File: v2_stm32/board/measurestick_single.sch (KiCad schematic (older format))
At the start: 5 parts, among them IC1 LM393, J1 USB_A

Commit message: STM32 board: Power supply
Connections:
- wire segments 24 -> 19
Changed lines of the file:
@@
 $Descr A4 11693 8268
 encoding utf-8
-Sheet 4 5
+Sheet 3 6
 Title ""
 Date ""
@@
 	1    0    0    -1
 $EndComp
-Wire Wire Line
-	4850 2700 4850 2750
-Wire Wire Line
-	4850 3350 4850 3400
 $Comp
 L power:GND #PWR?
 U 1 1 60261649
-P 4850 3400
+P 4850 3350
 AR Path="/60261649" Ref="#PWR?"  Part="1"
 AR Path="/6025D9E2/60261649" Ref="#PWR?"  Part="1"
@@
 AR Path="/60265FC9/60261649" Ref="#PWR?"  Part="1"
 AR Path="/6026601C/60261649" Ref="#PWR?"  Part="1"
-F 0 "#PWR?" H 4850 3150 50  0001 C CNN
-F 1 "GND" H 4855 3227 50  0000 C CNN
-F 2 "" H 4850 3400 50  0001 C CNN
-F 3 "" H 4850 3400 50  0001 C CNN
-	1    4850 3400
+F 0 "#PWR?" H 4850 3100 50  0001 C CNN
+F 1 "GND" H 4855 3177 50  0000 C CNN
+F 2 "" H 4850 3350 50  0001 C CNN
+F 3 "" H 4850 3350 50  0001 C CNN
+	1    4850 3350
 	1    0    0    -1
 $EndComp
@@
 L power:GND #PWR?
 U 1 1 60261663
-P 2300 3450
+P 2300 3400
 AR Path="/6025D9E2/60261663" Ref="#PWR?"  Part="1"
 AR Path="/6025D9E2/6025E7C0/60261663" Ref="#PWR01"  Part="1"
@@
 AR Path="/60265FC9/60261663" Ref="#PWR?"  Part="1"
 AR Path="/6026601C/60261663" Ref="#PWR?"  Part="1"
-F 0 "#PWR?" H 2300 3200 50  0001 C CNN
-F 1 "GND" H 2305 3277 50  0000 C CNN
-F 2 "" H 2300 3450 50  0001 C CNN
-F 3 "" H 2300 3450 50  0001 C CNN
-	1    2300 3450
-	1    0    0    -1
-$EndComp
-Wire Wire Line
-	2300 3400 2300 3450
+F 0 "#PWR?" H 2300 3150 50  0001 C CNN
+F 1 "GND" H 2305 3227 50  0000 C CNN
+F 2 "" H 2300 3400 50  0001 C CNN
+F 3 "" H 2300 3400 50  0001 C CNN
+	1    2300 3400
+	1    0    0    -1
+$EndComp
 Connection ~ 2300 3400
 Wire Wire Line
@@
 Text HLabel 4250 3450 2    50   Input ~ 0
 CLK
-$Comp
-L power:+3.3V #PWR?
-U 1 1 60261675
-P 4850 2700
-AR Path="/6025D9E2/60261675" Ref="#PWR?"  Part="1"
-AR Path="/6025D9E2/6025E7C0/60261675" Ref="#PWR05"  Part="1"
-AR Path="/6025D9E2/60265A76/60261675" Ref="#PWR?"  Part="1"
-AR Path="/6025D9E2/60265B58/60261675" Ref="#PWR?"  Part="1"
-AR Path="/6025D9E2/60265BB4/60261675" Ref="#PWR?"  Part="1"
-AR Path="/6025D9E2/60265C25/60261675" Ref="#PWR?"  Part="1"
-AR Path="/60265C89/60261675" Ref="#PWR?"  Part="1"
-AR Path="/60265F6D/60261675" Ref="#PWR?"  Part="1"
-AR Path="/60265FC9/60261675" Ref="#PWR?"  Part="1"
-AR Path="/6026601C/60261675" Ref="#PWR?"  Part="1"
-F 0 "#PWR?" H 4850 2550 50  0001 C CNN
-F 1 "+3.3V" H 4865 2873 50  0000 C CNN
-F 2 "" H 4850 2700 50  0001 C CNN
-F 3 "" H 4850 2700 50  0001 C CNN
-	1    4850 2700
-	1    0    0    -1
-$EndComp
 $Comp
 L Device:R R?
@@
 L power:+3.3V #PWR?
 U 1 1 60261690
-P 3400 2100
+P 3400 2150
 AR Path="/6025D9E2/60261690" Ref="#PWR?"  Part="1"
 AR Path="/6025D9E2/6025E7C0/60261690" Ref="#PWR03"  Part="1"
@@
 AR Path="/60265FC9/60261690" Ref="#PWR?"  Part="1"
 AR Path="/6026601C/60261690" Ref="#PWR?"  Part="1"
-F 0 "#PWR?" H 3400 1950 50  0001 C CNN
-F 1 "+3.3V" H 3415 2273 50  0000 C CNN
-F 2 "" H 3400 2100 50  0001 C CNN
-F 3 "" H 3400 2100 50  0001 C CNN
-	1    3400 2100
+F 0 "#PWR?" H 3400 2000 50  0001 C CNN
+F 1 "+3.3V" H 3415 2323 50  0000 C CNN
+F 2 "" H 3400 2150 50  0001 C CNN
+F 3 "" H 3400 2150 50  0001 C CNN
+	1    3400 2150
 	1    0    0    -1
 $EndComp
@@
 L power:GND #PWR?
 U 1 1 60261696
-P 3400 3950
+P 3400 3900
 AR Path="/60261696" Ref="#PWR?"  Part="1"
 AR Path="/6025D9E2/60261696" Ref="#PWR?"  Part="1"
@@
 AR Path="/60265FC9/60261696" Ref="#PWR?"  Part="1"
 AR Path="/6026601C/60261696" Ref="#PWR?"  Part="1"
-F 0 "#PWR?" H 3400 3700 50  0001 C CNN
-F 1 "GND" H 3405 3777 50  0000 C CNN
-F 2 "" H 3400 3950 50  0001 C CNN
-F 3 "" H 3400 3950 50  0001 C CNN
-	1    3400 3950
-	1    0    0    -1
-$EndComp
-Wire Wire Line
-	3400 3900 3400 3950
-Wire Wire Line
-	3400 2150 3400 2100
+F 0 "#PWR?" H 3400 3650 50  0001 C CNN
+F 1 "GND" H 3405 3727 50  0000 C CNN
+F 2 "" H 3400 3900 50  0001 C CNN
+F 3 "" H 3400 3900 50  0001 C CNN
+	1    3400 3900
+	1    0    0    -1
+$EndComp
 $Comp
 L Device:C C?
@@
 L power:+3.3V #PWR?
 U 1 1 602616A5
-P 5400 2700
+P 5400 2750
 AR Path="/6025D9E2/602616A5" Ref="#PWR?"  Part="1"
 AR Path="/6025D9E2/6025E7C0/602616A5" Ref="#PWR07"  Part="1"
@@
 AR Path="/60265FC9/602616A5" Ref="#PWR?"  Part="1"
 AR Path="/6026601C/602616A5" Ref="#PWR?"  Part="1"
-F 0 "#PWR?" H 5400 2550 50  0001 C CNN
-F 1 "+3.3V" H 5415 2873 50  0000 C CNN
-F 2 "" H 5400 2700 50  0001 C CNN
-F 3 "" H 5400 2700 50  0001 C CNN
-	1    5400 2700
+F 0 "#PWR?" H 5400 2600 50  0001 C CNN
+F 1 "+3.3V" H 5415 2923 50  0000 C CNN
+F 2 "" H 5400 2750 50  0001 C CNN
+F 3 "" H 5400 2750 50  0001 C CNN
+	1    5400 2750
 	1    0    0    -1
 $EndComp
@@
 L power:GND #PWR?
 U 1 1 602616AB
-P 5400 3400
+P 5400 3350
 AR Path="/602616AB" Ref="#PWR?"  Part="1"
 AR Path="/6025D9E2/602616AB" Ref="#PWR?"  Part="1"
@@
 AR Path="/60265FC9/602616AB" Ref="#PWR?"  Part="1"
 AR Path="/6026601C/602616AB" Ref="#PWR?"  Part="1"
-F 0 "#PWR?" H 5400 3150 50  0001 C CNN
-F 1 "GND" H 5405 3227 50  0000 C CNN
-F 2 "" H 5400 3400 50  0001 C CNN
-F 3 "" H 5400 3400 50  0001 C CNN
-	1    5400 3400
-	1    0    0    -1
-$EndComp
-Wire Wire Line
-	5400 3200 5400 3400
-Wire Wire Line
-	5400 2700 5400 2900
+F 0 "#PWR?" H 5400 3100 50  0001 C CNN
+F 1 "GND" H 5405 3177 50  0000 C CNN
+F 2 "" H 5400 3350 50  0001 C CNN
+F 3 "" H 5400 3350 50  0001 C CNN
+	1    5400 3350
+	1    0    0    -1
+$EndComp
+Wire Wire Line
+	5400 3200 5400 3350
+Wire Wire Line
+	5400 2750 5400 2900
+$Comp
+L power:+3.3V #PWR?
+U 1 1 60261675
+P 4850 2750
+AR Path="/6025D9E2/60261675" Ref="#PWR?"  Part="1"
+AR Path="/6025D9E2/6025E7C0/60261675" Ref="#PWR05"  Part="1"
+AR Path="/6025D9E2/60265A76/60261675" Ref="#PWR?"  Part="1"
+AR Path="/6025D9E2/60265B58/60261675" Ref="#PWR?"  Part="1"
+AR Path="/6025D9E2/60265BB4/60261675" Ref="#PWR?"  Part="1"
+AR Path="/6025D9E2/60265C25/60261675" Ref="#PWR?"  Part="1"
+AR Path="/60265C89/60261675" Ref="#PWR?"  Part="1"
+AR Path="/60265F6D/60261675" Ref="#PWR?"  Part="1"
+AR Path="/60265FC9/60261675" Ref="#PWR?"  Part="1"
+AR Path="/6026601C/60261675" Ref="#PWR?"  Part="1"
+F 0 "#PWR?" H 4850 2600 50  0001 C CNN
+F 1 "+3.3V" H 4865 2923 50  0000 C CNN
+F 2 "" H 4850 2750 50  0001 C CNN
+F 3 "" H 4850 2750 50  0001 C CNN
+	1    4850 2750
+	1    0    0    -1
+$EndComp
 $EndSCHEMATC

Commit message: Switched to 64 pin STM32F103. Assigned pins
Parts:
- J1: symbol Connector:USB_A -> lathecontrol_stm32-rescue:USB_A-Connector
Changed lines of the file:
@@
 IN_Clk
 $Comp
-L Connector:USB_A J?
+L lathecontrol_stm32-rescue:USB_A-Connector J?
 U 1 1 60261659
 P 2350 3000
@@
 AR Path="/60265FC9/60261659" Ref="J?"  Part="1"
 AR Path="/6026601C/60261659" Ref="J?"  Part="1"
+AR Path="/60261659" Ref="J?"  Part="1"
 F 0 "J?" H 2407 3467 50  0000 C CNN
 F 1 "USB_A" H 2407 3376 50  0000 C CNN

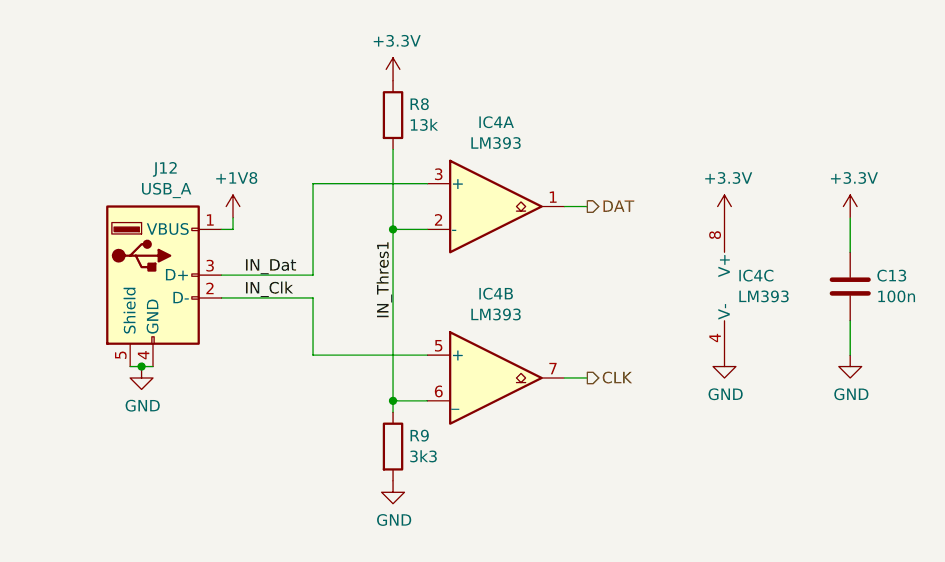
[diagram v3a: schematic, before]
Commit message: Added connectors
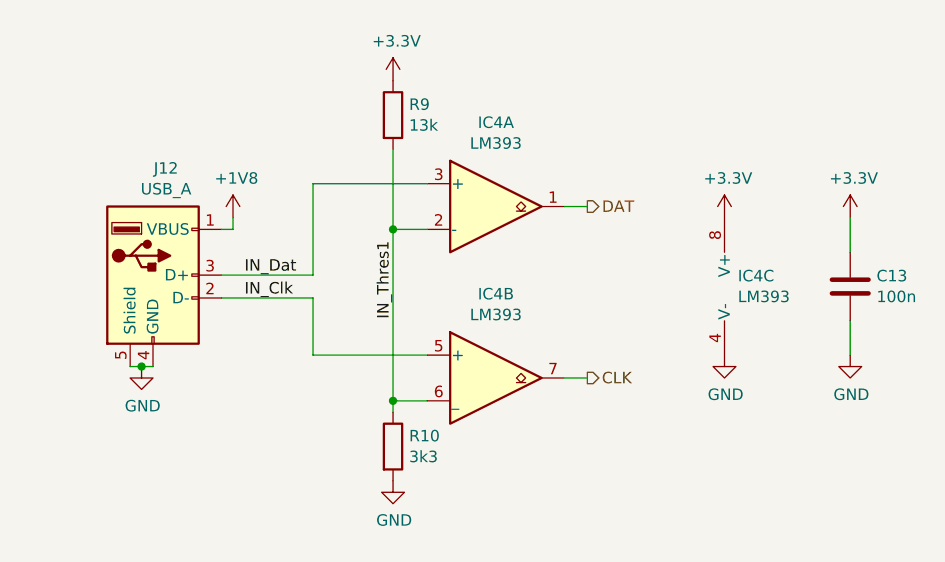
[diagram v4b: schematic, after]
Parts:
- renumbered C1 to C10, J1 to J9, R1 to R3, R2 to R4

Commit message: Added LEDs
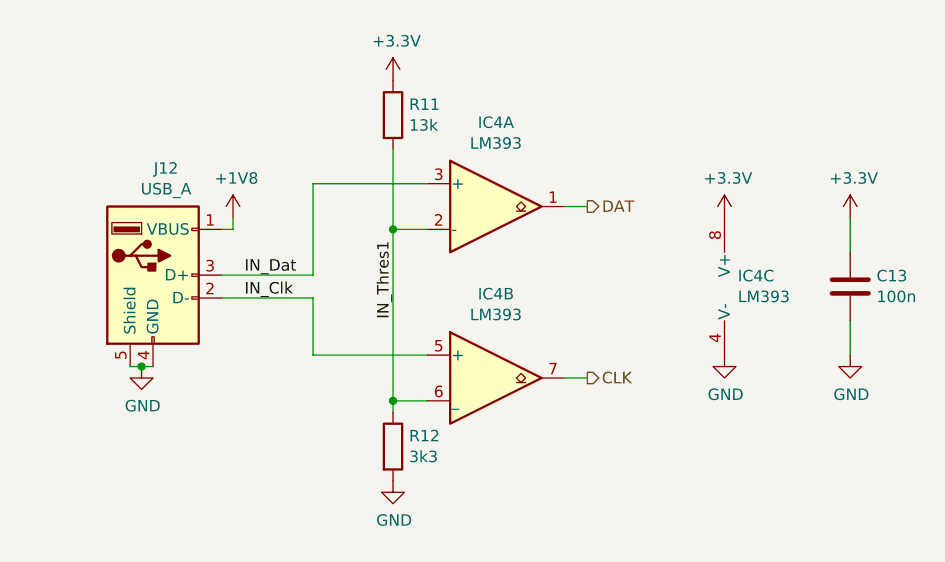
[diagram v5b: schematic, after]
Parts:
- renumbered R3 to R5, R4 to R6
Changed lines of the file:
@@
 AR Path="/6025D9E2/60265BB4/60261649" Ref="#PWR?"  Part="1"
 AR Path="/6025D9E2/60265C25/60261649" Ref="#PWR?"  Part="1"
-AR Path="/60265C89/60261649" Ref="#PWR040"  Part="1"
-AR Path="/60265F6D/60261649" Ref="#PWR048"  Part="1"
-AR Path="/60265FC9/60261649" Ref="#PWR056"  Part="1"
-AR Path="/6026601C/60261649" Ref="#PWR064"  Part="1"
-F 0 "#PWR064" H 4850 3100 50  0001 C CNN
+AR Path="/60265C89/60261649" Ref="#PWR042"  Part="1"
+AR Path="/60265F6D/60261649" Ref="#PWR050"  Part="1"
+AR Path="/60265FC9/60261649" Ref="#PWR058"  Part="1"
+AR Path="/6026601C/60261649" Ref="#PWR066"  Part="1"
+F 0 "#PWR066" H 4850 3100 50  0001 C CNN
 F 1 "GND" H 4855 3177 50  0000 C CNN
 F 2 "" H 4850 3350 50  0001 C CNN
@@
 AR Path="/6025D9E2/60265BB4/60261663" Ref="#PWR?"  Part="1"
 AR Path="/6025D9E2/60265C25/60261663" Ref="#PWR?"  Part="1"
-AR Path="/60265C89/60261663" Ref="#PWR035"  Part="1"
-AR Path="/60265F6D/60261663" Ref="#PWR043"  Part="1"
-AR Path="/60265FC9/60261663" Ref="#PWR051"  Part="1"
-AR Path="/6026601C/60261663" Ref="#PWR059"  Part="1"
-F 0 "#PWR059" H 2300 3150 50  0001 C CNN
+AR Path="/60265C89/60261663" Ref="#PWR037"  Part="1"
+AR Path="/60265F6D/60261663" Ref="#PWR045"  Part="1"
+AR Path="/60265FC9/60261663" Ref="#PWR053"  Part="1"
+AR Path="/6026601C/60261663" Ref="#PWR061"  Part="1"
+F 0 "#PWR061" H 2300 3150 50  0001 C CNN
 F 1 "GND" H 2305 3227 50  0000 C CNN
 F 2 "" H 2300 3400 50  0001 C CNN
@@
 AR Path="/6025D9E2/60265BB4/6026166C" Ref="#PWR?"  Part="1"
 AR Path="/6025D9E2/60265C25/6026166C" Ref="#PWR?"  Part="1"
-AR Path="/60265C89/6026166C" Ref="#PWR036"  Part="1"
-AR Path="/60265F6D/6026166C" Ref="#PWR044"  Part="1"
-AR Path="/60265FC9/6026166C" Ref="#PWR052"  Part="1"
-AR Path="/6026601C/6026166C" Ref="#PWR060"  Part="1"
-F 0 "#PWR060" H 2700 2600 50  0001 C CNN
+AR Path="/60265C89/6026166C" Ref="#PWR038"  Part="1"
+AR Path="/60265F6D/6026166C" Ref="#PWR046"  Part="1"
+AR Path="/60265FC9/6026166C" Ref="#PWR054"  Part="1"
+AR Path="/6026601C/6026166C" Ref="#PWR062"  Part="1"
+F 0 "#PWR062" H 2700 2600 50  0001 C CNN
 F 1 "+1V8" H 2715 2923 50  0000 C CNN
 F 2 "" H 2700 2750 50  0001 C CNN
@@
 AR Path="/6025D9E2/60265BB4/6026167C" Ref="R?"  Part="1"
 AR Path="/6025D9E2/60265C25/6026167C" Ref="R?"  Part="1"
-AR Path="/60265C89/6026167C" Ref="R3"  Part="1"
-AR Path="/60265F6D/6026167C" Ref="R5"  Part="1"
-AR Path="/60265FC9/6026167C" Ref="R7"  Part="1"
-AR Path="/6026601C/6026167C" Ref="R9"  Part="1"
-F 0 "R9" H 3470 2346 50  0000 L CNN
+AR Path="/60265C89/6026167C" Ref="R5"  Part="1"
+AR Path="/60265F6D/6026167C" Ref="R7"  Part="1"
+AR Path="/60265FC9/6026167C" Ref="R9"  Part="1"
+AR Path="/6026601C/6026167C" Ref="R11"  Part="1"
+F 0 "R11" H 3470 2346 50  0000 L CNN
 F 1 "13k" H 3470 2255 50  0000 L CNN
 F 2 "Resistor_SMD:R_0603_1608Metric" V 3330 2300 50  0001 C CNN
@@
 AR Path="/6025D9E2/60265BB4/60261683" Ref="R?"  Part="1"
 AR Path="/6025D9E2/60265C25/60261683" Ref="R?"  Part="1"
-AR Path="/60265C89/60261683" Ref="R4"  Part="1"
-AR Path="/60265F6D/60261683" Ref="R6"  Part="1"
-AR Path="/60265FC9/60261683" Ref="R8"  Part="1"
-AR Path="/6026601C/60261683" Ref="R10"  Part="1"
-F 0 "R10" H 3470 3796 50  0000 L CNN
+AR Path="/60265C89/60261683" Ref="R6"  Part="1"
+AR Path="/60265F6D/60261683" Ref="R8"  Part="1"
+AR Path="/60265FC9/60261683" Ref="R10"  Part="1"
+AR Path="/6026601C/60261683" Ref="R12"  Part="1"
+F 0 "R12" H 3470 3796 50  0000 L CNN
 F 1 "3k3" H 3470 3705 50  0000 L CNN
 F 2 "Resistor_SMD:R_0603_1608Metric" V 3330 3750 50  0001 C CNN
@@
 AR Path="/6025D9E2/60265BB4/60261690" Ref="#PWR?"  Part="1"
 AR Path="/6025D9E2/60265C25/60261690" Ref="#PWR?"  Part="1"
-AR Path="/60265C89/60261690" Ref="#PWR037"  Part="1"
-AR Path="/60265F6D/60261690" Ref="#PWR045"  Part="1"
-AR Path="/60265FC9/60261690" Ref="#PWR053"  Part="1"
-AR Path="/6026601C/60261690" Ref="#PWR061"  Part="1"
-F 0 "#PWR061" H 3400 2000 50  0001 C CNN
+AR Path="/60265C89/60261690" Ref="#PWR039"  Part="1"
+AR Path="/60265F6D/60261690" Ref="#PWR047"  Part="1"
+AR Path="/60265FC9/60261690" Ref="#PWR055"  Part="1"
+AR Path="/6026601C/60261690" Ref="#PWR063"  Part="1"
+F 0 "#PWR063" H 3400 2000 50  0001 C CNN
 F 1 "+3.3V" H 3415 2323 50  0000 C CNN
 F 2 "" H 3400 2150 50  0001 C CNN
@@
 AR Path="/6025D9E2/60265BB4/60261696" Ref="#PWR?"  Part="1"
 AR Path="/6025D9E2/60265C25/60261696" Ref="#PWR?"  Part="1"
-AR Path="/60265C89/60261696" Ref="#PWR038"  Part="1"
-AR Path="/60265F6D/60261696" Ref="#PWR046"  Part="1"
-AR Path="/60265FC9/60261696" Ref="#PWR054"  Part="1"
-AR Path="/6026601C/60261696" Ref="#PWR062"  Part="1"
-F 0 "#PWR062" H 3400 3650 50  0001 C CNN
+AR Path="/60265C89/60261696" Ref="#PWR040"  Part="1"
+AR Path="/60265F6D/60261696" Ref="#PWR048"  Part="1"
+AR Path="/60265FC9/60261696" Ref="#PWR056"  Part="1"
+AR Path="/6026601C/60261696" Ref="#PWR064"  Part="1"
+F 0 "#PWR064" H 3400 3650 50  0001 C CNN
 F 1 "GND" H 3405 3727 50  0000 C CNN
 F 2 "" H 3400 3900 50  0001 C CNN
@@
 AR Path="/6025D9E2/60265BB4/602616A5" Ref="#PWR?"  Part="1"
 AR Path="/6025D9E2/60265C25/602616A5" Ref="#PWR?"  Part="1"
-AR Path="/60265C89/602616A5" Ref="#PWR041"  Part="1"
-AR Path="/60265F6D/602616A5" Ref="#PWR049"  Part="1"
-AR Path="/60265FC9/602616A5" Ref="#PWR057"  Part="1"
-AR Path="/6026601C/602616A5" Ref="#PWR065"  Part="1"
-F 0 "#PWR065" H 5400 2600 50  0001 C CNN
+AR Path="/60265C89/602616A5" Ref="#PWR043"  Part="1"
+AR Path="/60265F6D/602616A5" Ref="#PWR051"  Part="1"
+AR Path="/60265FC9/602616A5" Ref="#PWR059"  Part="1"
+AR Path="/6026601C/602616A5" Ref="#PWR067"  Part="1"
+F 0 "#PWR067" H 5400 2600 50  0001 C CNN
 F 1 "+3.3V" H 5415 2923 50  0000 C CNN
 F 2 "" H 5400 2750 50  0001 C CNN
@@
 AR Path="/6025D9E2/60265BB4/602616AB" Ref="#PWR?"  Part="1"
 AR Path="/6025D9E2/60265C25/602616AB" Ref="#PWR?"  Part="1"
-AR Path="/60265C89/602616AB" Ref="#PWR042"  Part="1"
-AR Path="/60265F6D/602616AB" Ref="#PWR050"  Part="1"
-AR Path="/60265FC9/602616AB" Ref="#PWR058"  Part="1"
-AR Path="/6026601C/602616AB" Ref="#PWR066"  Part="1"
-F 0 "#PWR066" H 5400 3100 50  0001 C CNN
+AR Path="/60265C89/602616AB" Ref="#PWR044"  Part="1"
+AR Path="/60265F6D/602616AB" Ref="#PWR052"  Part="1"
+AR Path="/60265FC9/602616AB" Ref="#PWR060"  Part="1"
+AR Path="/6026601C/602616AB" Ref="#PWR068"  Part="1"
+F 0 "#PWR068" H 5400 3100 50  0001 C CNN
 F 1 "GND" H 5405 3177 50  0000 C CNN
 F 2 "" H 5400 3350 50  0001 C CNN
@@
 AR Path="/6025D9E2/60265BB4/60261675" Ref="#PWR?"  Part="1"
 AR Path="/6025D9E2/60265C25/60261675" Ref="#PWR?"  Part="1"
-AR Path="/60265C89/60261675" Ref="#PWR039"  Part="1"
-AR Path="/60265F6D/60261675" Ref="#PWR047"  Part="1"
-AR Path="/60265FC9/60261675" Ref="#PWR055"  Part="1"
-AR Path="/6026601C/60261675" Ref="#PWR063"  Part="1"
-F 0 "#PWR063" H 4850 2600 50  0001 C CNN
+AR Path="/60265C89/60261675" Ref="#PWR041"  Part="1"
+AR Path="/60265F6D/60261675" Ref="#PWR049"  Part="1"
+AR Path="/60265FC9/60261675" Ref="#PWR057"  Part="1"
+AR Path="/6026601C/60261675" Ref="#PWR065"  Part="1"
+F 0 "#PWR065" H 4850 2600 50  0001 C CNN
 F 1 "+3.3V" H 4865 2923 50  0000 C CNN
 F 2 "" H 4850 2750 50  0001 C CNN

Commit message: Schematic finished (V0.1), Added footprints
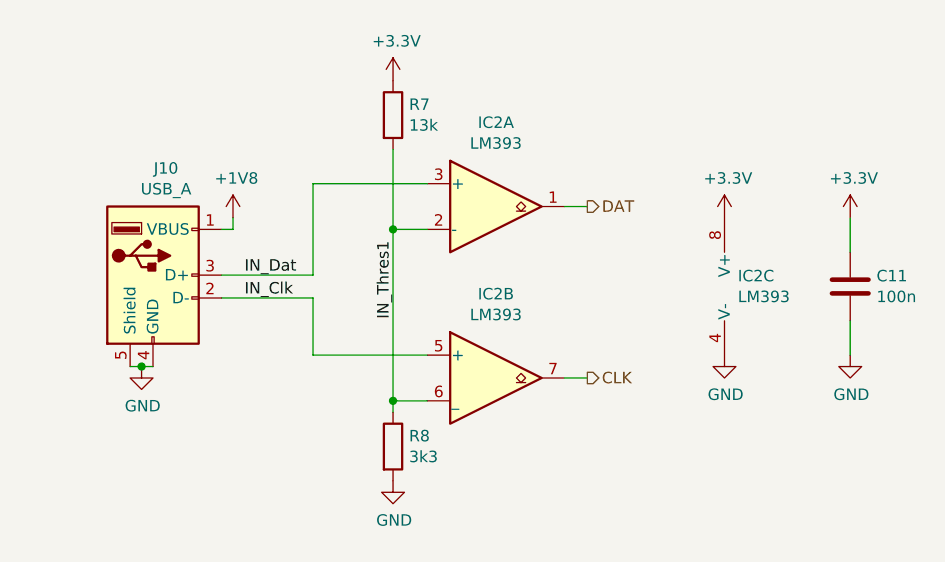
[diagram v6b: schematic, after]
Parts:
- J9: footprint Connector_USB:USB_A_Wuerth_614004134726_Horizontal -> Lathecontrol_STM32:USB_A_Upright_C26235
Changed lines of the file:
@@
 $Descr A4 11693 8268
 encoding utf-8
-Sheet 4 7
+Sheet 3 7
 Title ""
 Date ""
@@
 AR Path="/60265FC9/60261634" Ref="IC3"  Part="2"
 AR Path="/6026601C/60261634" Ref="IC4"  Part="2"
-F 0 "IC4" H 3850 3817 50  0000 C CNN
+F 0 "IC2" H 3850 3817 50  0000 C CNN
 F 1 "LM393" H 3850 3726 50  0000 C CNN
 F 2 "Package_SO:SOIC-8_3.9x4.9mm_P1.27mm" H 3850 3450 50  0001 C CNN
@@
 AR Path="/60265FC9/6026163B" Ref="IC3"  Part="1"
 AR Path="/6026601C/6026163B" Ref="IC4"  Part="1"
-F 0 "IC4" H 3850 3067 50  0000 C CNN
+F 0 "IC2" H 3850 3067 50  0000 C CNN
 F 1 "LM393" H 3850 2976 50  0000 C CNN
 F 2 "Package_SO:SOIC-8_3.9x4.9mm_P1.27mm" H 3850 2700 50  0001 C CNN
@@
 AR Path="/60265FC9/60261641" Ref="IC3"  Part="3"
 AR Path="/6026601C/60261641" Ref="IC4"  Part="3"
-F 0 "IC4" H 4908 3096 50  0000 L CNN
+F 0 "IC2" H 4908 3096 50  0000 L CNN
 F 1 "LM393" H 4908 3005 50  0000 L CNN
 F 2 "Package_SO:SOIC-8_3.9x4.9mm_P1.27mm" H 4950 3050 50  0001 C CNN
@@
 AR Path="/6026601C/60261659" Ref="J12"  Part="1"
 AR Path="/60261659" Ref="J?"  Part="1"
-F 0 "J12" H 2407 3467 50  0000 C CNN
+F 0 "J10" H 2407 3467 50  0000 C CNN
 F 1 "USB_A" H 2407 3376 50  0000 C CNN
-F 2 "Connector_USB:USB_A_Wuerth_614004134726_Horizontal" H 2500 2950 50  0001 C CNN
+F 2 "Lathecontrol_STM32:USB_A_Upright_C26235" H 2500 2950 50  0001 C CNN
 F 3 "https://datasheet.lcsc.com/szlcsc/1811131821_Jing-Extension-of-the-Electronic-Co-C26235_C26235.pdf" H 2500 2950 50  0001 C CNN
 F 4 "C26235" H 2350 3000 50  0001 C CNN "LCSC"
@@
 AR Path="/60265FC9/6026167C" Ref="R9"  Part="1"
 AR Path="/6026601C/6026167C" Ref="R11"  Part="1"
-F 0 "R11" H 3470 2346 50  0000 L CNN
+F 0 "R7" H 3470 2346 50  0000 L CNN
 F 1 "13k" H 3470 2255 50  0000 L CNN
 F 2 "Resistor_SMD:R_0603_1608Metric" V 3330 2300 50  0001 C CNN
@@
 AR Path="/60265FC9/60261683" Ref="R10"  Part="1"
 AR Path="/6026601C/60261683" Ref="R12"  Part="1"
-F 0 "R12" H 3470 3796 50  0000 L CNN
+F 0 "R8" H 3470 3796 50  0000 L CNN
 F 1 "3k3" H 3470 3705 50  0000 L CNN
 F 2 "Resistor_SMD:R_0603_1608Metric" V 3330 3750 50  0001 C CNN
@@
 AR Path="/60265FC9/6026169F" Ref="C12"  Part="1"
 AR Path="/6026601C/6026169F" Ref="C13"  Part="1"
-F 0 "C13" H 5515 3096 50  0000 L CNN
+F 0 "C11" H 5515 3096 50  0000 L CNN
 F 1 "100n" H 5515 3005 50  0000 L CNN
 F 2 "Capacitor_SMD:C_0603_1608Metric" H 5438 2900 50  0001 C CNN
